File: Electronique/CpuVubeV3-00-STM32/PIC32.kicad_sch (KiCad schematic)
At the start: 26 parts, among them Q201 BSS123, U201 MCP1501-SN, U202 PIC32MX795F512L

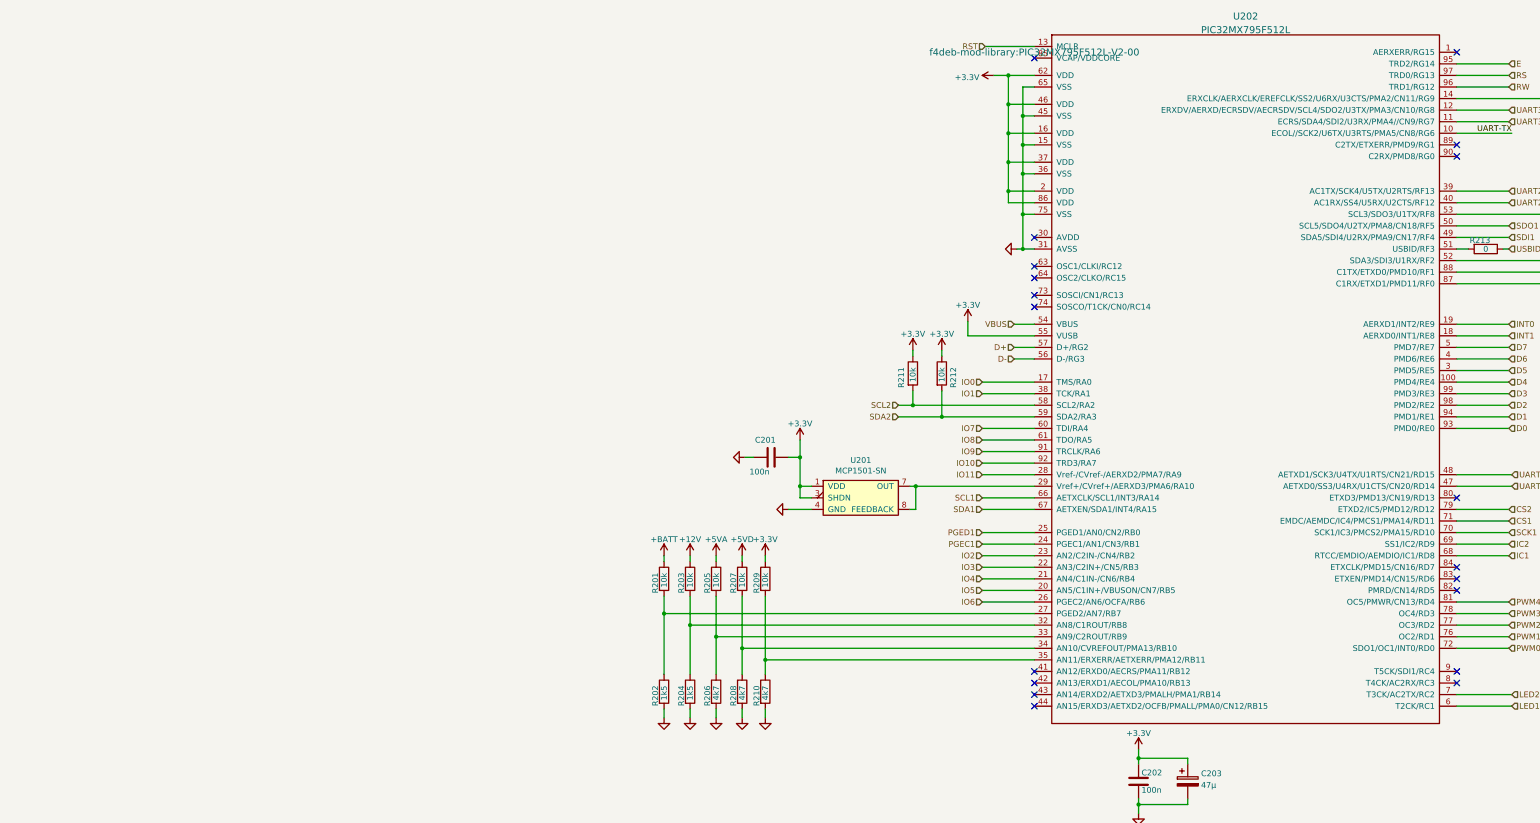
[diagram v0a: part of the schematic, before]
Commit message: CPUCube V3-00 STM32
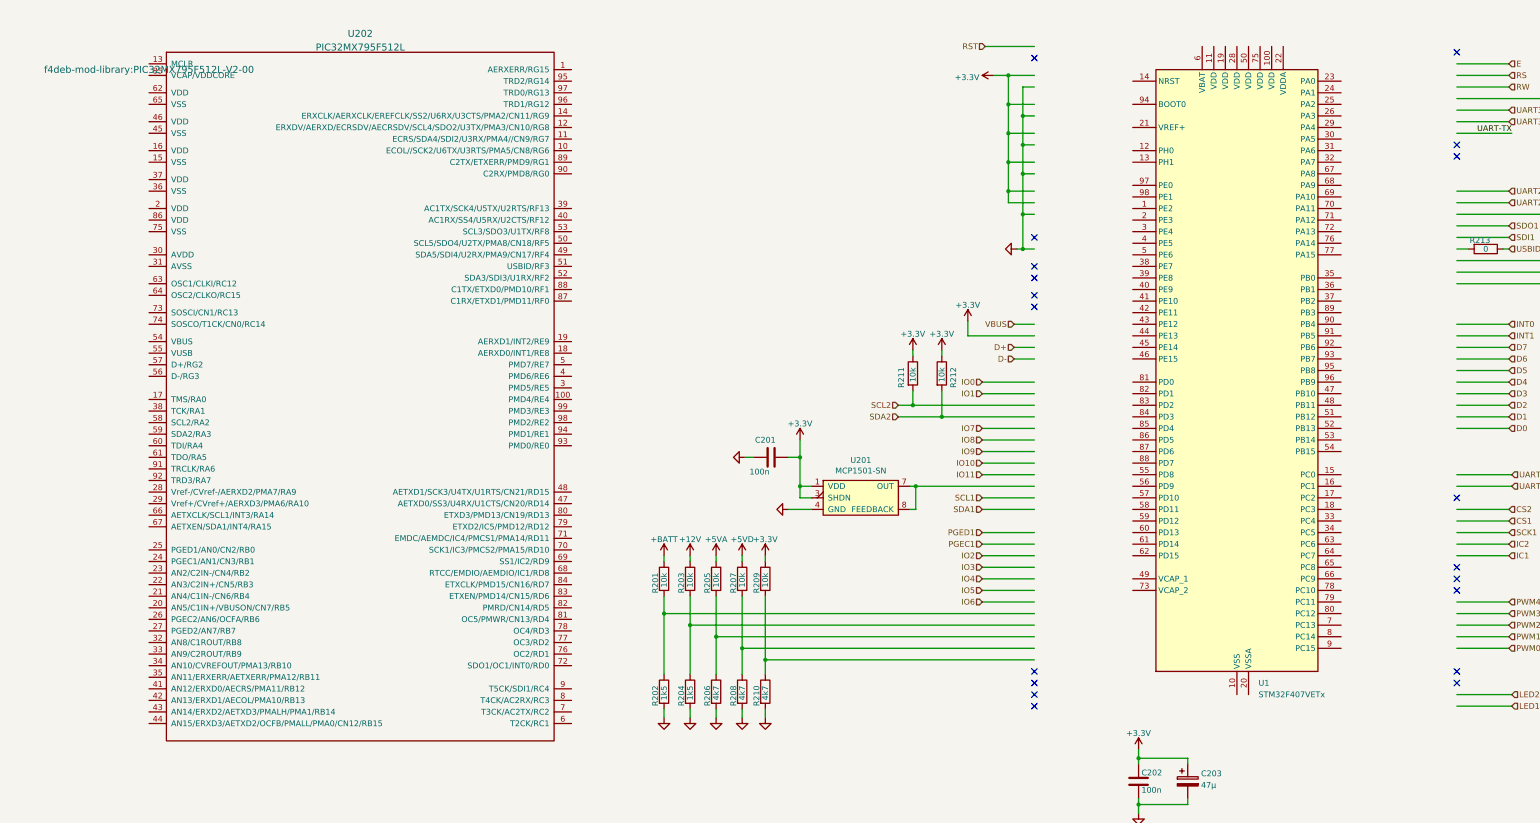
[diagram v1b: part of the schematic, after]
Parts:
- added U1: STM32F407VETx, Package_QFP:LQFP-100_14x14mm_P0.5mm, symbol MCU_ST_STM32F4:STM32F407VETx
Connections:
- net +3V3: no longer U202.16 (VDD), U202.2 (VDD), U202.37 (VDD), U202.46 (VDD), U202.55 (VUSB), U202.62 (VDD), U202.86 (VDD)
- net CAN1RX: no longer U202.87 (C1RX/ETXD1/PMD11/RF0)
- net CAN1TX: no longer U202.88 (C1TX/ETXD0/PMD10/RF1)
- net CS1: no longer U202.71 (EMDC/AEMDC/IC4/PMCS1/PMA14/RD11)
- net CS2: no longer U202.79 (ETXD2/IC5/PMD12/RD12)
- net D+: no longer U202.57 (D+/RG2)
- net D-: no longer U202.56 (D-/RG3)
- net D0: no longer U202.93 (PMD0/RE0)
- net D1: no longer U202.94 (PMD1/RE1)
- net D2: no longer U202.98 (PMD2/RE2)
- net D3: no longer U202.99 (PMD3/RE3)
- net D4: no longer U202.100 (PMD4/RE4)
- net D5: no longer U202.3 (PMD5/RE5)
- net D6: no longer U202.4 (PMD6/RE6)
- net D7: no longer U202.5 (PMD7/RE7)
- net E: no longer U202.95 (TRD2/RG14)
- net GND: no longer U202.15 (VSS), U202.31 (AVSS), U202.36 (VSS), U202.45 (VSS), U202.65 (VSS), U202.75 (VSS)
- net IC1: no longer U202.68 (RTCC/EMDIO/AEMDIO/IC1/RD8)
- net IC2: no longer U202.69 (SS1/IC2/RD9)
- net INT0: no longer U202.19 (AERXD1/INT2/RE9)
- net INT1: no longer U202.18 (AERXD0/INT1/RE8)
- net IO0: no longer U202.17 (TMS/RA0)
- net IO1: no longer U202.38 (TCK/RA1)
- net IO10: no longer U202.92 (TRD3/RA7)
- net IO11: no longer U202.28 (Vref-/CVref-/AERXD2/PMA7/RA9)
- net IO2: no longer U202.23 (AN2/C2IN-/CN4/RB2)
- net IO3: no longer U202.22 (AN3/C2IN+/CN5/RB3)
- net IO4: no longer U202.21 (AN4/C1IN-/CN6/RB4)
- net IO5: no longer U202.20 (AN5/C1IN+/VBUSON/CN7/RB5)
- net IO6: no longer U202.26 (PGEC2/AN6/OCFA/RB6)
- net IO7: no longer U202.60 (TDI/RA4)
- net IO8: no longer U202.61 (TDO/RA5)
- net IO9: no longer U202.91 (TRCLK/RA6)
- net LED1: no longer U202.6 (T2CK/RC1)
- net LED2: no longer U202.7 (T3CK/AC2TX/RC2)
- net PGEC1: no longer U202.24 (PGEC1/AN1/CN3/RB1)
- net PGED1: no longer U202.25 (PGED1/AN0/CN2/RB0)
- net PWM0: no longer U202.72 (SDO1/OC1/INT0/RD0)
- net PWM1: no longer U202.76 (OC2/RD1)
- net PWM2: no longer U202.77 (OC3/RD2)
- net PWM3: no longer U202.78 (OC4/RD3)
- net PWM4: no longer U202.81 (OC5/PMWR/CN13/RD4)
- net RS: no longer U202.97 (TRD0/RG13)
- net RST: no longer U202.13 (MCLR)
- net RW: no longer U202.96 (TRD1/RG12)
- net SCK1: no longer U202.70 (SCK1/IC3/PMCS2/PMA15/RD10)
- net SCL1: no longer U202.66 (AETXCLK/SCL1/INT3/RA14)
- net SCL2: no longer U202.58 (SCL2/RA2)
- net SCL3: no longer U202.53 (SCL3/SDO3/U1TX/RF8)
- net SDA1: no longer U202.67 (AETXEN/SDA1/INT4/RA15)
- net SDA2: no longer U202.59 (SDA2/RA3)
- net SDA3: no longer U202.52 (SDA3/SDI3/U1RX/RF2)
- net SDI1: no longer U202.49 (SDA5/SDI4/U2RX/PMA9/CN17/RF4)
- net SDO1: no longer U202.50 (SCL5/SDO4/U2TX/PMA8/CN18/RF5)
- net UART-TX: no longer U202.10 (ECOL//SCK2/U6TX/U3RTS/PMA5/CN8/RG6)
- net UART1-RX: no longer U202.47 (AETXD0/SS3/U4RX/U1CTS/CN20/RD14)
- net UART1-TX: no longer U202.48 (AETXD1/SCK3/U4TX/U1RTS/CN21/RD15)
- net UART2-RX: no longer U202.40 (AC1RX/SS4/U5RX/U2CTS/RF12)
- net UART2-TX: no longer U202.39 (AC1TX/SCK4/U5TX/U2RTS/RF13)
- net UART3-RX: no longer U202.11 (ECRS/SDA4/SDI2/U3RX/PMA4//CN9/RG7)
- net UART3-TX: no longer U202.12 (ERXDV/AERXD/ECRSDV/AECRSDV/SCL4/SDO2/U3TX/PMA3/CN10/RG8)
- net VBUS: no longer U202.54 (VBUS)
- net at U201.7 (OUT), U201.8 (FEEDBACK): no longer U202.29 (Vref+/CVref+/AERXD3/PMA6/RA10)
- net at R216.2, R217.1: no longer U202.14 (ERXCLK/AERXCLK/EREFCLK/SS2/U6RX/U3CTS/PMA2/CN11/RG9)
- net at R201.2, R202.1: no longer U202.27 (PGED2/AN7/RB7)
- net at R209.2, R210.1: no longer U202.35 (AN11/ERXERR/AETXERR/PMA12/RB11)
- net at R213.2: no longer U202.51 (USBID/RF3)
- net at R203.2, R204.1: no longer U202.32 (AN8/C1ROUT/RB8)
- net at R205.2, R206.1: no longer U202.33 (AN9/C2ROUT/RB9)
- net at R207.2, R208.1: no longer U202.34 (AN10/CVREFOUT/PMA13/RB10)
- new net: U1.10 (VSS), U1.27 (VSS), U1.74 (VSS), U1.99 (VSS)
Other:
- moved on the sheet: U202

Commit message: MAJ Schema
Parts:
- removed C202: 100n, Capacitor_SMD:C_0603_1608Metric, symbol Device:C
- removed C203: 47µ, Capacitor_Tantalum_SMD:CP_EIA-7343-30_AVX-N_Pad2.25x2.55mm_HandSolder, symbol Device:C_Polarized
- added C202, C203: 100n, Capacitor_SMD:C_0603_1608Metric, symbol Device:C_Small
- added C204, C205: 2.2UF, Capacitor_SMD:C_1206_3216Metric, symbol Device:C_Small
- added C211: 10n, Capacitor_SMD:C_0603_1608Metric, symbol Device:C_Small
- added C213: 1UF, Capacitor_Tantalum_SMD:CP_EIA-3216-10_Kemet-I_Pad1.58x1.35mm_HandSolder, symbol Device:C_Polarized_Small
- added Y201: 32.768Khz, symbol Device:Crystal
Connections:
- net GND: now also U1.10 (VSS), U1.20 (VSSA), U1.27 (VSS), U1.74 (VSS), U1.99 (VSS), C202.2, C203.2, C204.2, C205.2, C211.2, C213.2
- net RST: now also U1.14 (NRST)
- net at U201.7 (OUT), U201.8 (FEEDBACK): now also U1.21 (VREF+), C211.1, C213.1
- net +3.3V: now reaches U1.100 (VDD)
- net +3.3V: now also U1.11 (VDD), U1.19 (VDD), U1.22 (VDDA), U1.28 (VDD), U1.50 (VDD), U1.75 (VDD)
- net at U1.49 (VCAP_1): now also C204.1
- net at U1.73 (VCAP_2): now also C205.1
- net at U1.8 (PC14): now also C202.1, Y201.1
- net at U1.9 (PC15): now also C203.1, Y201.2
- no-connect marks 19 -> 13
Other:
- moved on the sheet: C201, U1, U201
